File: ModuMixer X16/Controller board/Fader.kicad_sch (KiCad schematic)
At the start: 8 parts, among them J8 Screw_Terminal_01x02, J9 Screw_Terminal_01x03, U8 DRV8833PWP

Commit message: update idk
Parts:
- added C71: 10u, Capacitor_SMD:C_0603_1608Metric, symbol Device:C
- renumbered C45 to C69, C46 to C70, J8 to J7, J9 to J8, R9 to R13, U8 to U10
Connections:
- net 5V_MAIN: now also C71.1
- net GND: now also C71.2
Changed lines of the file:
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@@
+		)
+	)
+	(label "5V_MAIN"
+		(at 106.68 57.15 180)
+		(fields_autoplaced yes)
+		(effects
+			(font
+				(size 1.27 1.27)
+			)
+			(justify right bottom)
 		)
 	)
@@
 		(dnp no)
 		(fields_autoplaced yes)
-		(property "Reference" "U8"
+		(property "Reference" "U10"
 			(at 58.0741 59.69 0)
 			(effects
@@
 			(project "ModuMixer X16"
 				(path "/1d80c8ed-e175-4f30-b143-8bf97252529d/9cb4a910-e6cc-4057-93b6-8f2942eae9a7"
-					(reference "U8")
+					(reference "U10")
 					(unit 1)
 				)
@@
 		(dnp no)
 		(fields_autoplaced yes)
-		(property "Reference" "#PWR078"
+		(property "Reference" "#PWR097"
 			(at 55.88 68.58 0)
 			(effects
@@
 			(project "ModuMixer X16"
 				(path "/1d80c8ed-e175-4f30-b143-8bf97252529d/9cb4a910-e6cc-4057-93b6-8f2942eae9a7"
-					(reference "#PWR078")
+					(reference "#PWR097")
 					(unit 1)
 				)
@@
 		(dnp no)
 		(fields_autoplaced yes)
-		(property "Reference" "R9"
+		(property "Reference" "R13"
 			(at 109.2199 22.86 0)
 			(effects
@@
 			(project "ModuMixer X16"
 				(path "/1d80c8ed-e175-4f30-b143-8bf97252529d/9cb4a910-e6cc-4057-93b6-8f2942eae9a7"
-					(reference "R9")
+					(reference "R13")
 					(unit 1)
 				)
@@
 		(dnp no)
 		(fields_autoplaced yes)
-		(property "Reference" "C46"
+		(property "Reference" "C70"
 			(at 109.2199 41.91 0)
 			(effects
@@
 			(project "ModuMixer X16"
 				(path "/1d80c8ed-e175-4f30-b143-8bf97252529d/9cb4a910-e6cc-4057-93b6-8f2942eae9a7"
-					(reference "C46")
+					(reference "C70")
 					(unit 1)
 				)
@@
 		(dnp no)
 		(fields_autoplaced yes)
-		(property "Reference" "#PWR080"
+		(property "Reference" "#PWR098"
 			(at 87.63 97.79 0)
 			(effects
@@
 			(project "ModuMixer X16"
 				(path "/1d80c8ed-e175-4f30-b143-8bf97252529d/9cb4a910-e6cc-4057-93b6-8f2942eae9a7"
-					(reference "#PWR080")
+					(reference "#PWR098")
 					(unit 1)
 				)
@@
 		(dnp no)
 		(fields_autoplaced yes)
-		(property "Reference" "C45"
+		(property "Reference" "C69"
 			(at 109.2199 31.75 0)
 			(effects
@@
 			(project "ModuMixer X16"
 				(path "/1d80c8ed-e175-4f30-b143-8bf97252529d/9cb4a910-e6cc-4057-93b6-8f2942eae9a7"
-					(reference "C45")
+					(reference "C69")
+					(unit 1)
+				)
+			)
+		)
+	)
+	(symbol
+		(lib_id "power:GND")
+		(at 114.3 57.15 90)
+		(unit 1)
+		(exclude_from_sim no)
+		(in_bom yes)
+		(on_board yes)
+		(dnp no)
+		(fields_autoplaced yes)
+		(property "Reference" "#PWR0100"
+			(at 120.65 57.15 0)
+			(effects
+				(font
+					(size 1.27 1.27)
+				)
+				(hide yes)
+			)
+		)
+		(property "Value" "GND"
+			(at 119.38 57.15 0)
+			(effects
+				(font
+					(size 1.27 1.27)
+				)
+			)
+		)
+		(property "Footprint" ""
+			(at 114.3 57.15 0)
+			(effects
+				(font
+					(size 1.27 1.27)
+				)
+				(hide yes)
+			)
+		)
+		(property "Datasheet" ""
+			(at 114.3 57.15 0)
+			(effects
+				(font
+					(size 1.27 1.27)
+				)
+				(hide yes)
+			)
+		)
+		(property "Description" "Power symbol creates a global label with name \"GND\" , ground"
+			(at 114.3 57.15 0)
+			(effects
+				(font
+					(size 1.27 1.27)
+				)
+				(hide yes)
+			)
+		)
+		(pin "1"
+		)
+		(instances
+			(project "ModuMixer X16"
+				(path "/1d80c8ed-e175-4f30-b143-8bf97252529d/9cb4a910-e6cc-4057-93b6-8f2942eae9a7"
+					(reference "#PWR0100")
 					(unit 1)
 				)
@@
 		(dnp no)
 		(fields_autoplaced yes)
-		(property "Reference" "J8"
+		(property "Reference" "J7"
 			(at 100.33 60.9599 0)
 			(effects
@@
 			(project "ModuMixer X16"
 				(path "/1d80c8ed-e175-4f30-b143-8bf97252529d/9cb4a910-e6cc-4057-93b6-8f2942eae9a7"
-					(reference "J8")
+					(reference "J7")
 					(unit 1)
 				)
@@
 		(dnp no)
 		(fields_autoplaced yes)
-		(property "Reference" "#PWR077"
+		(property "Reference" "#PWR096"
 			(at 34.29 41.91 0)
 			(effects
@@
 			(project "ModuMixer X16"
 				(path "/1d80c8ed-e175-4f30-b143-8bf97252529d/9cb4a910-e6cc-4057-93b6-8f2942eae9a7"
-					(reference "#PWR077")
+					(reference "#PWR096")
 					(unit 1)
 				)
@@
 		(dnp no)
 		(fields_autoplaced yes)
-		(property "Reference" "J9"
+		(property "Reference" "J8"
 			(at 100.33 74.9299 0)
 			(effects
@@
 			(project "ModuMixer X16"
 				(path "/1d80c8ed-e175-4f30-b143-8bf97252529d/9cb4a910-e6cc-4057-93b6-8f2942eae9a7"
-					(reference "J9")
+					(reference "J8")
 					(unit 1)
 				)
@@
 		(dnp no)
 		(fields_autoplaced yes)
-		(property "Reference" "#PWR079"
+		(property "Reference" "#PWR099"
 			(at 120.65 35.56 0)
 			(effects
@@
 			(project "ModuMixer X16"
 				(path "/1d80c8ed-e175-4f30-b143-8bf97252529d/9cb4a910-e6cc-4057-93b6-8f2942eae9a7"
-					(reference "#PWR079")
+					(reference "#PWR099")
+					(unit 1)
+				)
+			)
+		)
+	)
+	(symbol
+		(lib_id "Device:C")
+		(at 110.49 57.15 90)
+		(unit 1)
+		(exclude_from_sim no)
+		(in_bom yes)
+		(on_board yes)
+		(dnp no)
+		(fields_autoplaced yes)
+		(property "Reference" "C71"
+			(at 110.49 49.53 90)
+			(effects
+				(font
+					(size 1.27 1.27)
+				)
+			)
+		)
+		(property "Value" "10u"
+			(at 110.49 52.07 90)
+			(effects
+				(font
+					(size 1.27 1.27)
+				)
+			)
+		)
+		(property "Footprint" "Capacitor_SMD:C_0603_1608Metric"
+			(at 114.3 56.1848 0)
+			(effects
+				(font
+					(size 1.27 1.27)
+				)
+				(hide yes)
+			)
+		)
+		(property "Datasheet" "~"
+			(at 110.49 57.15 0)
+			(effects
+				(font
+					(size 1.27 1.27)
+				)
+				(hide yes)
+			)
+		)
+		(property "Description" "Unpolarized capacitor"
+			(at 110.49 57.15 0)
+			(effects
+				(font
+					(size 1.27 1.27)
+				)
+				(hide yes)
+			)
+		)
+		(pin "2"
+		)
+		(pin "1"
+		)
+		(instances
+			(project "ModuMixer X16"
+				(path "/1d80c8ed-e175-4f30-b143-8bf97252529d/9cb4a910-e6cc-4057-93b6-8f2942eae9a7"
+					(reference "C71")
 					(unit 1)
 				)
@@
 		(dnp no)
 		(fields_autoplaced yes)
-		(property "Reference" "#PWR076"
+		(property "Reference" "#PWR095"
 			(at 34.29 39.37 0)
 			(effects
@@
 			(project "ModuMixer X16"
 				(path "/1d80c8ed-e175-4f30-b143-8bf97252529d/9cb4a910-e6cc-4057-93b6-8f2942eae9a7"
-					(reference "#PWR076")
-					(unit 1)
-				)
+					(reference "#PWR095")
+					(unit 1)
+				)

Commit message: Midway through MCU replacement
Sometimes i feel like it would be better to start over considering it's a digital mixer.
The only thing left is doing the DSP connections and calculating the values for a 16mhz crystal on all 3 MCUs
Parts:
- renumbered C69 to C40, C70 to C41, C71 to C42, J7 to J5, J8 to J6, JP8 to JP5, JP9 to JP6, R13 to R17, U10 to U12
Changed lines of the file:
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@@
 		(dnp no)
 		(fields_autoplaced yes)
-		(property "Reference" "U10"
+		(property "Reference" "U12"
 			(at 58.0741 59.69 0)
 			(effects
@@
 			(project "ModuMixer X16"
 				(path "/1d80c8ed-e175-4f30-b143-8bf97252529d/9cb4a910-e6cc-4057-93b6-8f2942eae9a7"
-					(reference "U10")
+					(reference "U12")
 					(unit 1)
 				)
@@
 		(dnp no)
 		(fields_autoplaced yes)
-		(property "Reference" "#PWR097"
+		(property "Reference" "#PWR0108"
 			(at 55.88 68.58 0)
 			(effects
@@
 			(project "ModuMixer X16"
 				(path "/1d80c8ed-e175-4f30-b143-8bf97252529d/9cb4a910-e6cc-4057-93b6-8f2942eae9a7"
-					(reference "#PWR097")
+					(reference "#PWR0108")
 					(unit 1)
 				)
@@
 		(dnp no)
 		(fields_autoplaced yes)
-		(property "Reference" "R13"
+		(property "Reference" "R17"
 			(at 109.2199 22.86 0)
 			(effects
@@
 			(project "ModuMixer X16"
 				(path "/1d80c8ed-e175-4f30-b143-8bf97252529d/9cb4a910-e6cc-4057-93b6-8f2942eae9a7"
-					(reference "R13")
+					(reference "R17")
 					(unit 1)
 				)
@@
 		(dnp no)
 		(fields_autoplaced yes)
-		(property "Reference" "C70"
+		(property "Reference" "C41"
 			(at 109.2199 41.91 0)
 			(effects
@@
 			(project "ModuMixer X16"
 				(path "/1d80c8ed-e175-4f30-b143-8bf97252529d/9cb4a910-e6cc-4057-93b6-8f2942eae9a7"
-					(reference "C70")
+					(reference "C41")
 					(unit 1)
 				)
@@
 		(dnp no)
 		(fields_autoplaced yes)
-		(property "Reference" "JP8"
+		(property "Reference" "JP5"
 			(at 97.79 82.55 0)
 			(effects
@@
 			(project "ModuMixer X16"
 				(path "/1d80c8ed-e175-4f30-b143-8bf97252529d/9cb4a910-e6cc-4057-93b6-8f2942eae9a7"
-					(reference "JP8")
+					(reference "JP5")
 					(unit 1)
 				)
@@
 		(dnp no)
 		(fields_autoplaced yes)
-		(property "Reference" "#PWR098"
+		(property "Reference" "#PWR0109"
 			(at 87.63 97.79 0)
 			(effects
@@
 			(project "ModuMixer X16"
 				(path "/1d80c8ed-e175-4f30-b143-8bf97252529d/9cb4a910-e6cc-4057-93b6-8f2942eae9a7"
-					(reference "#PWR098")
+					(reference "#PWR0109")
 					(unit 1)
 				)
@@
 		(dnp no)
 		(fields_autoplaced yes)
-		(property "Reference" "C69"
+		(property "Reference" "C40"
 			(at 109.2199 31.75 0)
 			(effects
@@
 			(project "ModuMixer X16"
 				(path "/1d80c8ed-e175-4f30-b143-8bf97252529d/9cb4a910-e6cc-4057-93b6-8f2942eae9a7"
-					(reference "C69")
+					(reference "C40")
 					(unit 1)
 				)
@@
 		(dnp no)
 		(fields_autoplaced yes)
-		(property "Reference" "#PWR0100"
+		(property "Reference" "#PWR0111"
 			(at 120.65 57.15 0)
 			(effects
@@
 			(project "ModuMixer X16"
 				(path "/1d80c8ed-e175-4f30-b143-8bf97252529d/9cb4a910-e6cc-4057-93b6-8f2942eae9a7"
-					(reference "#PWR0100")
+					(reference "#PWR0111")
 					(unit 1)
 				)
@@
 		(dnp no)
 		(fields_autoplaced yes)
-		(property "Reference" "J7"
+		(property "Reference" "J5"
 			(at 100.33 60.9599 0)
 			(effects
@@
 			(project "ModuMixer X16"
 				(path "/1d80c8ed-e175-4f30-b143-8bf97252529d/9cb4a910-e6cc-4057-93b6-8f2942eae9a7"
-					(reference "J7")
+					(reference "J5")
 					(unit 1)
 				)
@@
 		(dnp no)
 		(fields_autoplaced yes)
-		(property "Reference" "#PWR096"
+		(property "Reference" "#PWR0107"
 			(at 34.29 41.91 0)
 			(effects
@@
 			(project "ModuMixer X16"
 				(path "/1d80c8ed-e175-4f30-b143-8bf97252529d/9cb4a910-e6cc-4057-93b6-8f2942eae9a7"
-					(reference "#PWR096")
+					(reference "#PWR0107")
 					(unit 1)
 				)
@@
 		(dnp no)
 		(fields_autoplaced yes)
-		(property "Reference" "J8"
+		(property "Reference" "J6"
 			(at 100.33 74.9299 0)
 			(effects
@@
 			(project "ModuMixer X16"
 				(path "/1d80c8ed-e175-4f30-b143-8bf97252529d/9cb4a910-e6cc-4057-93b6-8f2942eae9a7"
-					(reference "J8")
+					(reference "J6")
 					(unit 1)
 				)
@@
 		(dnp no)
 		(fields_autoplaced yes)
-		(property "Reference" "JP9"
+		(property "Reference" "JP6"
 			(at 97.79 91.44 0)
 			(effects
@@
 			(project "ModuMixer X16"
 				(path "/1d80c8ed-e175-4f30-b143-8bf97252529d/9cb4a910-e6cc-4057-93b6-8f2942eae9a7"
-					(reference "JP9")
+					(reference "JP6")
 					(unit 1)
 				)
@@
 		(dnp no)
 		(fields_autoplaced yes)
-		(property "Reference" "#PWR099"
+		(property "Reference" "#PWR0110"
 			(at 120.65 35.56 0)
 			(effects
@@
 			(project "ModuMixer X16"
 				(path "/1d80c8ed-e175-4f30-b143-8bf97252529d/9cb4a910-e6cc-4057-93b6-8f2942eae9a7"
-					(reference "#PWR099")
+					(reference "#PWR0110")
 					(unit 1)
 				)
@@
 		(dnp no)
 		(fields_autoplaced yes)
-		(property "Reference" "C71"
+		(property "Reference" "C42"
 			(at 110.49 49.53 90)
 			(effects
@@
 			(project "ModuMixer X16"
 				(path "/1d80c8ed-e175-4f30-b143-8bf97252529d/9cb4a910-e6cc-4057-93b6-8f2942eae9a7"
-					(reference "C71")
+					(reference "C42")
 					(unit 1)
 				)
@@
 		(dnp no)
 		(fields_autoplaced yes)
-		(property "Reference" "#PWR095"
+		(property "Reference" "#PWR0106"
 			(at 34.29 39.37 0)
 			(effects
@@
 			(project "ModuMixer X16"
 				(path "/1d80c8ed-e175-4f30-b143-8bf97252529d/9cb4a910-e6cc-4057-93b6-8f2942eae9a7"
-					(reference "#PWR095")
-					(unit 1)
-				)
+					(reference "#PWR0106")
+					(unit 1)
+				)

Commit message: asdasgashg
sfjhadgdjasdg
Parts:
- removed J5: Screw_Terminal_01x02, TerminalBlock:TerminalBlock_Xinya_XY308-2.54-2P_1x02_P2.54mm_Horizontal, symbol Connector:Screw_Terminal_01x02
- removed J6: Screw_Terminal_01x03, TerminalBlock:TerminalBlock_Xinya_XY308-2.54-3P_1x03_P2.54mm_Horizontal, symbol Connector:Screw_Terminal_01x03
- added J7: Conn_02x03_Counter_Clockwise, Connector_PinHeader_2.54mm:PinHeader_2x03_P2.54mm_Vertical, symbol Connector_Generic:Conn_02x03_Counter_Clockwise
- renumbered C40 to C63, C41 to C64, C42 to C65, JP5 to JP6, JP6 to JP7, R17 to R22
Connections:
- net FADER_A: now also J7.4 (Pin_4)
- net FADER_B: now also J7.5 (Pin_5)
- net FADER_MOTOR_OUT1: now also J7.1 (Pin_1)
- net FADER_MOTOR_OUT2: now also J7.2 (Pin_2)
- net FADER_W: now also J7.3 (Pin_3)

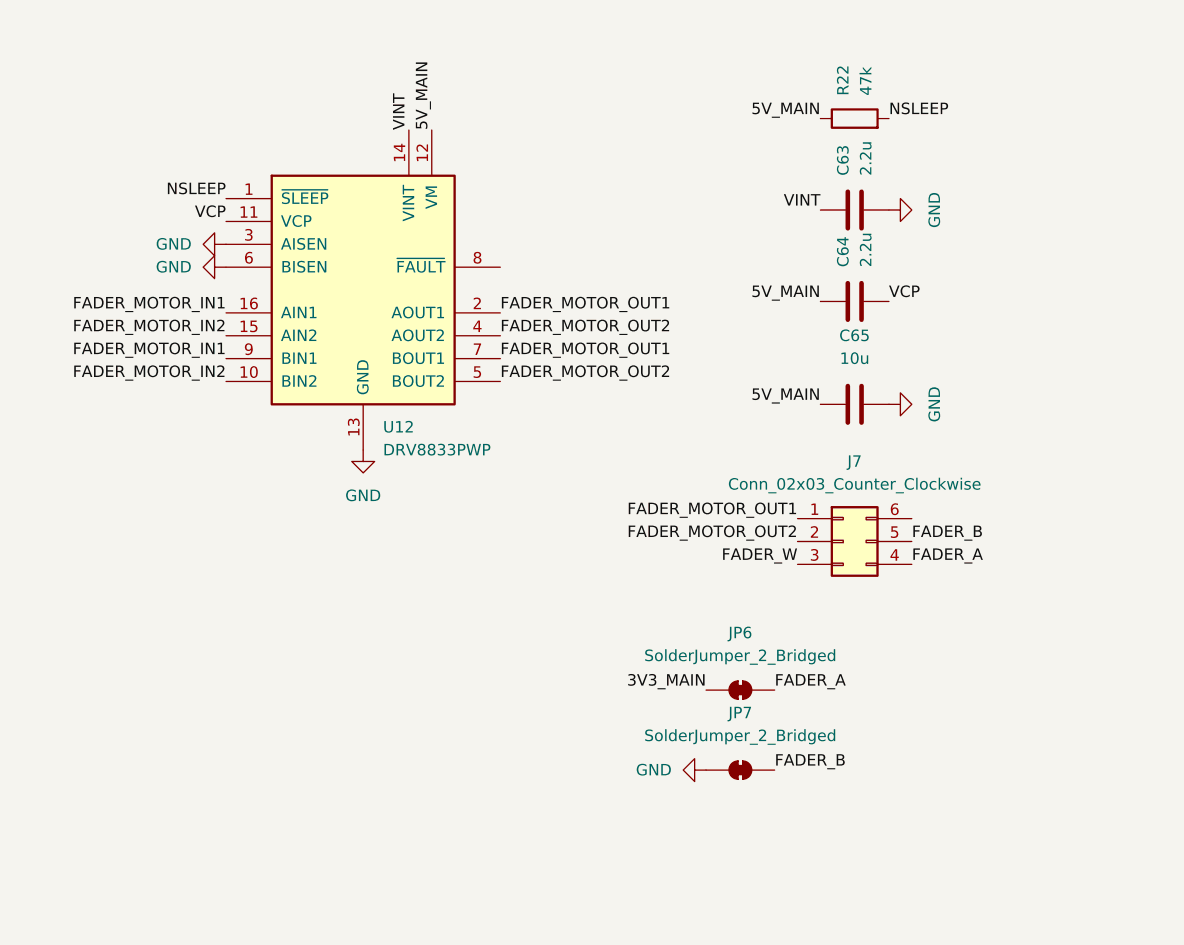
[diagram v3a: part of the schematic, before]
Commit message: Changed all labels to global
I made it in a rather hacky way (editing all files on notepad with Ctrl + H), i'm only reverting this if something breaks
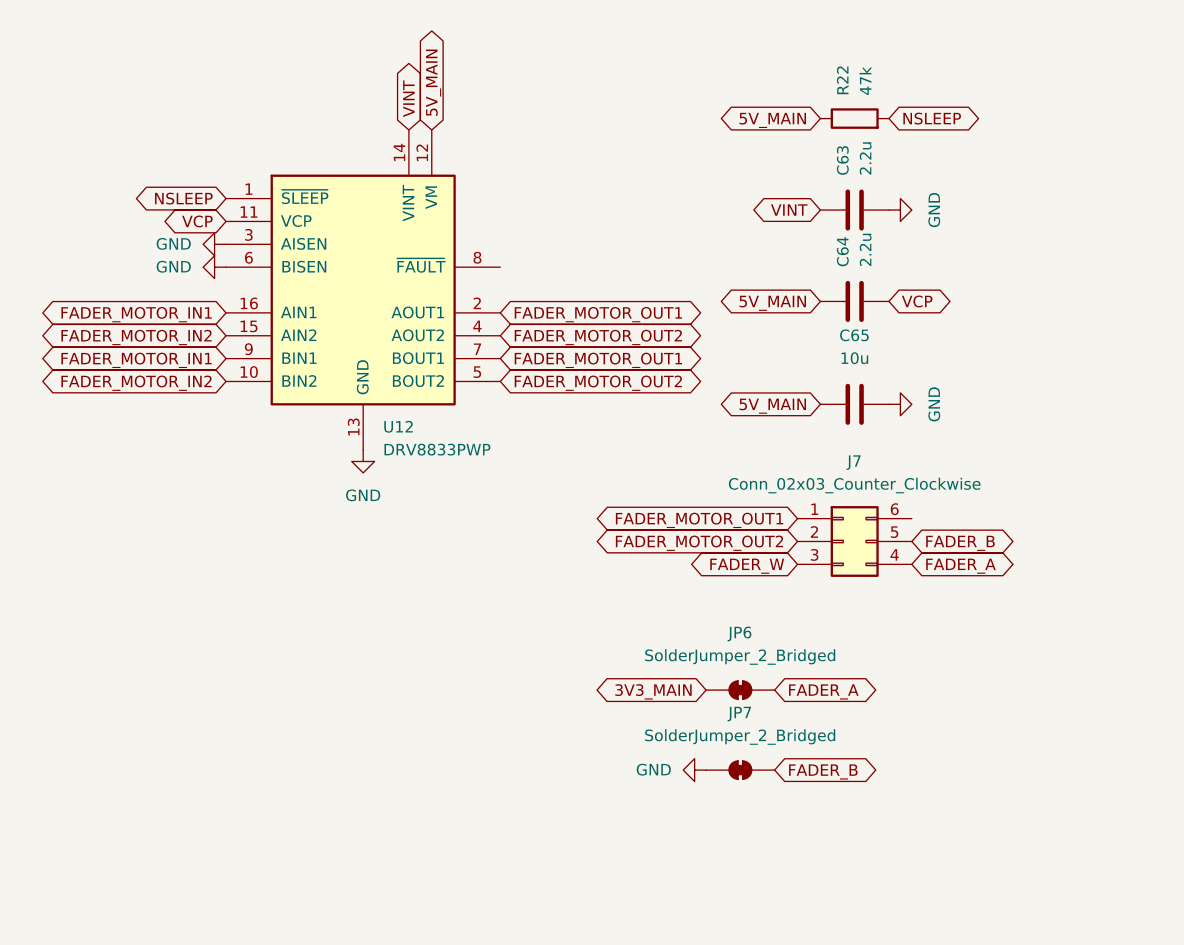
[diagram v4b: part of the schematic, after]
